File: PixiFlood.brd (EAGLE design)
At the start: 43.2 x 46 mm, 36 parts, among them IC1 WS2811-SOP8, IC2 78L05Z, T1 2N3904, T2 2N3904, T3 2N3904, U1 PT4115B89E, U2 PT4115B89E, U3 PT4115B89E, X2 22-23-2041

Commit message: Initial Commit
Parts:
- removed T$1, T$2, T$3, T$4, T$5, T$6, T$7, T$8, T$9: TEST_PINTP-2, headers:TP-2
- removed T1, T2, T3: 2N3904, transistor:TO92
- removed X2: 22-23-2041, connectors:22-23-2041
- added C3: .1uF, capacitors:EIA3216
- added C4: 10uF, capacitors:VISHAY-CASE-D
- added IC3: TC7W04FP-0.65, logic:SSOP8-0.65P-(TSSOP8)
- added TP1, TP2, TP3, TP4, TP5, TP6, TP7, TP9: TPSQTP15R, testpad:TP15R
- added TP8: TPSQTP20SQ, testpad:TP20SQ
- added X1: 22-23-2041, connectors:22-23-2041
- B1: value LED-BOARDNODIM -> LED-BOARDV4; device myBoards:LED_BOARD_V5_A -> special:LED_BOARD-V4
- C1: value 100uF -> 10uF; device rcl:TT2D6L -> capacitors:VISHAY-CASE-D
- C2: value .1uF -> 10uF; device rcl:C050-024X044 -> capacitors:VISHAY-CASE-D
- D1, D2, D3: value 1N5819 -> B340A; device diode:DO07 -> SparkFun-DiscreteSemi:SMA-DIODE
- IC1: value WS2811-SOP8 -> 78L05SMD; device MyLibrary:SO08-SKINNYPADS -> regulators:SO08
- IC2: value 78L05Z -> WS2811S; device linear:TO92 -> drivers:SO08
- L1, L2, L3: value INDUCTOR82114R -> SLF7045T-101MR60-H; device rcl:82114R-C -> inductors:SLF7045
- R1: value .3R -> .33R; device resistor:0204/7 -> resistor:R1210
- R2, R3: value .3R -> 33R; device resistor:0204/7 -> rcl:R1206
- R4: value 4.7k -> 100; device resistor:0204/7 -> rcl:R1206
- R5, R6: value 4.7k -> .33R; device resistor:0204/7 -> resistor:R1210
- R7, R9: value 33R -> 4.7k; device rcl:0204/7 -> rcl:R1206
- R8: value 100R -> 4.7k; device rcl:0204/7 -> rcl:R1206
- moved R3 31.3 mm to (39.9, 42.2)
- moved C2 22.5 mm to (22.0, 14.0), turned to 0 degrees
- moved R2 21.2 mm to (36.4, 42.0)
- moved R1 16.8 mm to (27.8, 26.2)
- moved R4 13.8 mm to (33.1, 42.0), flipped to the top
- moved R5 13.8 mm to (27.8, 17.7), flipped to the top, turned to 270 degrees
- moved IC1 13.7 mm to (24.4, 36.2), turned to 90 degrees
- moved R6 13.6 mm to (27.9, 9.43), flipped to the top
- moved R7 11.1 mm to (31.0, 34.0)
- moved C1 8.82 mm to (21.8, 22.4), turned to 0 degrees
- moved IC2 8.57 mm to (38.0, 36.3), turned to 0 degrees
- moved U3 8.46 mm to (32.1, 9.52)
- moved U2 8.22 mm to (32.1, 17.9)
- moved U1 7.73 mm to (32.1, 26.3)
- moved L3 7.47 mm to (38.6, 6.22), turned to 0 degrees
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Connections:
- removed net +12V: C1.+, D1.C, D2.C, D3.C, IC2.3, R1.1, R2.1, R3.1, T$9.P$1, U1.5, U2.5, U3.5, X2.1
- removed net DIN-R: IC1.6, R9.2
- removed net DO-R: IC1.5, R7.2
- removed net N$15: IC1.3, R6.2, T$5.P$1, T3.2
- removed net N$18: IC1.2, R5.2, T$4.P$1, T2.2
- removed net N$20: IC1.1, R4.2, T$1.P$1, T1.2
- new net BLU-WS: IC2.3, IC3.1, R7.2, TP2.TP
- new net DIN-E: R2.1, X1.3
- new net DO-E: R3.1, X1.4
- new net GREN-WS: IC2.2, IC3.6, R8.2, TP3.TP
- new net RED-WS: IC2.1, IC3.3, R9.2, TP7.TP
- new net VIN: C1.1, C2.1, C4.1, D1.C, D2.C, D3.C, IC1.8, R1.2, R5.2, R6.2, TP4.TP, U1.5, U2.5, U3.5, X1.1
- net +5V: now also C3.A, IC1.1, IC3.8, R7.1, R9.1, TP5.TP; no longer C2.1, IC2.1, R5.1, R6.1, T$2.P$1
- net BLUE: now also IC3.7, TP9.TP; no longer T$6.P$1, T3.1
- net BOUT: now also R6.1; no longer R3.2
- net DIN: now also IC2.6, R2.2; no longer R9.1, X2.3
- net DO: now also IC2.5, R3.2; no longer R7.1, X2.4
- net GND: now also C1.2, C3.C, C4.2, IC1.2, IC1.3, IC1.6, IC1.7, IC2.4, IC3.4, TP8.TP, X1.2; no longer C1.-, IC1.4, IC2.2, T$3.P$1, T1.3, T2.3, T3.3, X2.2
- net GOUT: now also R5.1; no longer R2.2
- net GREEN: now also IC3.2, TP6.TP; no longer T$7.P$1, T2.1
- net N$1: no longer L1.1@A
- net N$10: no longer L3.2@A
- net N$2: no longer L3.1@A
- net N$3: no longer L1.2@A
- net N$5: no longer L2.1@A
- net N$9: no longer L2.2@A
- net RED: now also IC3.5, TP1.TP; no longer T$8.P$1, T1.1
- net ROUT: now also R1.1; no longer R1.2
- net VDD: now also IC2.8, R4.2; no longer IC1.8, R8.2
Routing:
- net +12V: track 99.4 -> 0.00 mm
- net VIN: track 0.00 -> 78.1 mm, vias 0 -> 5
- net N$15: track 37.8 -> 0.00 mm, vias 1 -> 0
- net +5V: track 51.6 -> 29.6 mm
- net N$20: track 19.3 -> 0.00 mm
- net RED-WS: track 0.00 -> 16.9 mm
- net N$18: track 16.3 -> 0.00 mm
- net GREN-WS: track 0.00 -> 15.8 mm
- net BLU-WS: track 0.00 -> 14.3 mm
- net RED: track 21.0 -> 8.58 mm
- net DIN-E: track 0.00 -> 11.8 mm
- net DO-E: track 0.00 -> 11.6 mm
- net DO-R: track 11.1 -> 0.00 mm
- net ROUT: track 39.7 -> 50.7 mm
- net BLUE: track 17.7 -> 26.8 mm, vias 0 -> 2
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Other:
- board size 43.2 x 46 mm -> 43 x 46 mm
- board text added: "+"
- board text added: "-"
- board text added: "12v"
- board text added: "B"
- board text added: "DI"
- board text added: "G"
- board text added: "PixiFlood 10W"
- board text added: "R"
- board text added: "v2.0"
- board text removed: "12V"
- board text removed: "DIN"
- board text removed: "GND"
- board text removed: "PixiFlood"
- board text removed: "V1.11"

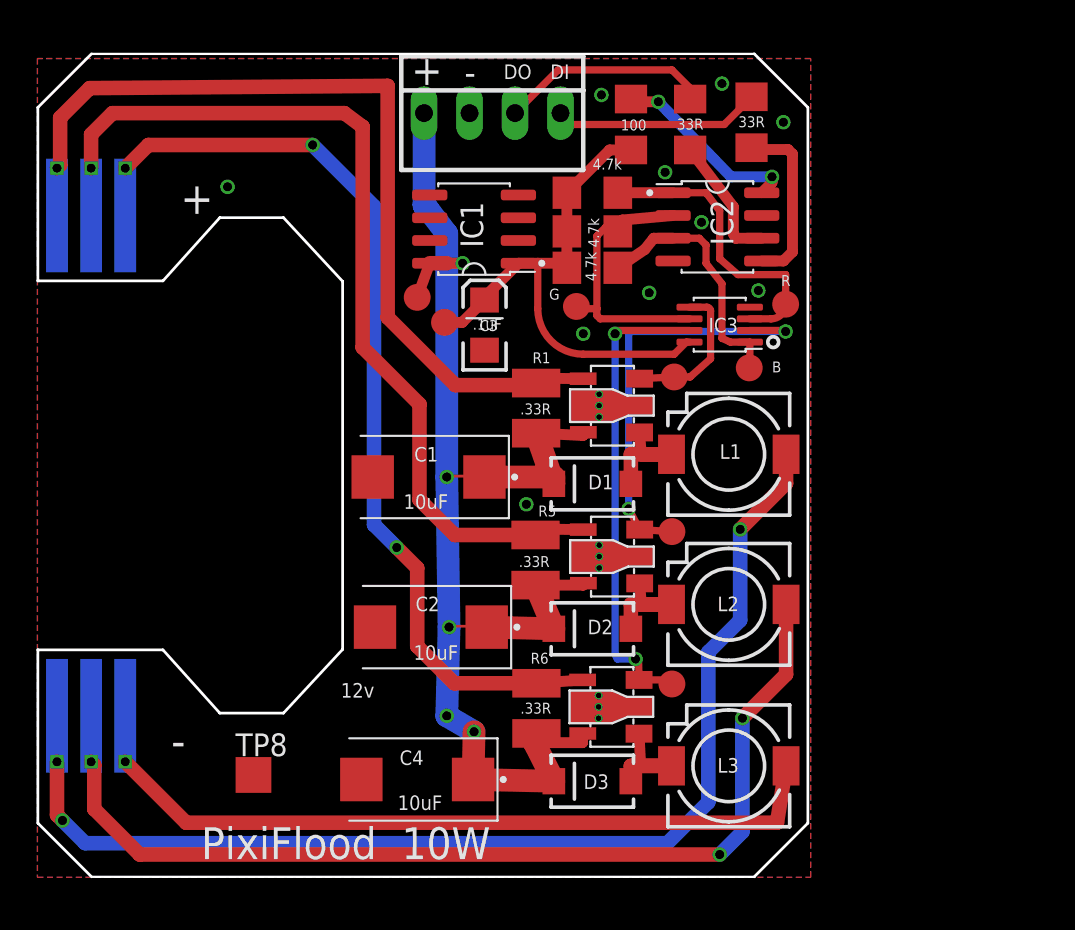
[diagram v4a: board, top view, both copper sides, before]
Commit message: Reworked layout
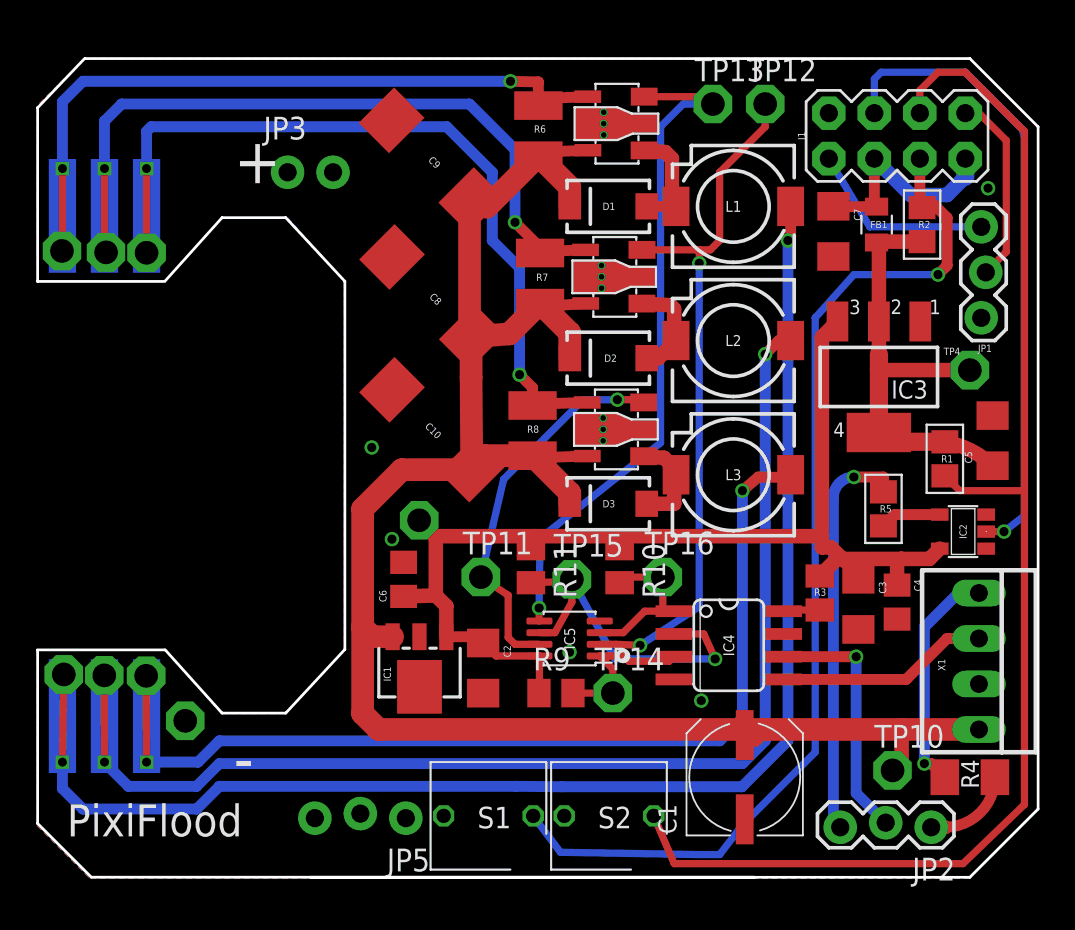
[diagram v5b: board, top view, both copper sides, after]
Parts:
- added C10, C8, C9: 10uF, rcl:SMC_D
- added C5, C7: 10uF, rcl:C1206
- added C6: .1uF, rcl:C0805
- added FB1: BLM21PG221SN1D, ELL-i-Passives:SMD0805-A
- added IC4: WS2811SOP8, drivers:SOP08-P-1.27
- added IC5: TC7W04FP-0.65, logic:SSOP8-0.65P-(TSSOP8)
- added J1: (no value), connectors:2X4
- added JP1, JP2: (no value), connectors:1X03_LOCK
- added JP3: M02NO_SILK, connectors:1X02_NO_SILK
- added JP5: (no value), connectors:1X03_LOCK_NO_SILK
- added R10, R11: 4.7kohm, rcl:M0805
- added S1, S2: SP, switch:TACT_5MM
- added TP10, TP11, TP12, TP13, TP14, TP15, TP16: TPSQPAD1-13, testpad:P1-13
- B1: value LED-BOARDV4 -> LED-BOARDRF; device special:LED_BOARD-V4 -> myBoards:RF_BOARD
- C1: value 10uF -> (none); device capacitors:VISHAY-CASE-D -> rcl:UD-6,3X5,8_NICHICON
- C2: device capacitors:VISHAY-CASE-D -> rcl:C1206
- C3: value .1uF -> 10uF; device capacitors:EIA3216 -> rcl:C1206
- C4: value 10uF -> .1uF; device capacitors:VISHAY-CASE-D -> rcl:C0805
- D1, D2, D3: value B340A -> MBRA140
- IC1: value 78L05SMD -> L78LXXCU/BU; device regulators:SO08 -> regulators:SOT89
- IC2: value WS2811S -> 74LVC1G125DBV; device drivers:SO08 -> logic:SOT23-5
- IC3: value TC7W04FP-0.65 -> LM1117-SOT223; device logic:SSOP8-0.65P-(TSSOP8) -> regulators:SOT223
- R1: value .33R -> 10K; device resistor:R1210 -> resistors:R0805
- R2: value 33R -> 10K; device rcl:R1206 -> resistors:R0805
- R3: value 33R -> 100ohm; device rcl:R1206 -> rcl:M0805
- R4: value 100 -> 33R; device rcl:R1206 -> rcl:M1206
- R5: value .33R -> 100; device resistor:R1210 -> resistors:R0805
- R6: value .33R -> .3ohm .25w; device resistor:R1210 -> rcl:R1210
- R7: value 4.7k -> .3hm .25w; device rcl:R1206 -> rcl:R1210
- R8: value 4.7k -> .3ohm .25w; device rcl:R1206 -> rcl:R1210
- R9: value 4.7k -> 4.7kohm; device rcl:R1206 -> rcl:M0805
- TP1, TP2, TP3, TP4, TP5, TP6, TP7, TP9: value TPSQTP15R -> TPSQPAD1-13; device testpad:TP15R -> testpad:P1-13
- TP8: value TPSQTP20SQ -> TPSQPAD1-13; device testpad:TP20SQ -> testpad:P1-13
- moved R4 41.1 mm to (52.1, 5.59), turned to 0 degrees
- moved X1 40.9 mm to (52.6, 12.1), turned to 270 degrees
- moved TP2 37.2 mm to (8.26, 8.74), turned to 180 degrees
- moved TP7 35.8 mm to (6.10, 34.9)
- moved TP9 34.0 mm to (1.47, 11.3), turned to 180 degrees
- moved R6 32.3 mm to (28.0, 41.7)
- moved TP4 31.1 mm to (52.1, 28.3)
- moved TP6 30.4 mm to (6.07, 11.3)
- moved TP3 28.9 mm to (1.37, 35.0)
- moved C4 28.6 mm to (48.0, 15.4), turned to 270 degrees
- moved R9 28.0 mm to (29.0, 10.3)
- moved R3 26.6 mm to (43.7, 15.9), turned to 90 degrees
- moved C3 26.1 mm to (45.8, 15.2), turned to 270 degrees
- moved IC1 24.7 mm to (21.3, 11.7), turned to 180 degrees
- moved C1 24.3 mm to (39.5, 5.59), turned to 90 degrees
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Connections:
- removed net BLU-WS: IC2.3, IC3.1, R7.2, TP2.TP
- removed net DIN-E: R2.1, X1.3
- removed net DO-E: R3.1, X1.4
- removed net GREN-WS: IC2.2, IC3.6, R8.2, TP3.TP
- removed net N$10: B1.B-, B1.B-@1, L3.2
- removed net N$9: B1.G-, B1.G-@1, L2.2
- removed net RED-WS: IC2.1, IC3.3, R9.2, TP7.TP
- removed net VIN: C1.1, C2.1, C4.1, D1.C, D2.C, D3.C, IC1.8, R1.2, R5.2, R6.2, TP4.TP, U1.5, U2.5, U3.5, X1.1
- new net +12V: C1.+, C10.+, C8.+, C9.+, D1.C, D2.C, D3.C, IC1.3, R6.2, R7.2, R8.2, TP10.TP, U1.5, U2.5, U3.5, X1.4
- new net +3V3: C5.1, FB1.P$1, IC3.2, IC3.4, R1.2, R2.1, TP4.TP
- new net DIN-W: R4.1, X1.1
- new net GPIO0: J1.6, R1.1, S2.1
- new net GPIO2: IC2.2, J1.4
- new net LED-B-NEG: B1.B-2, B1.B-@1, L3.2, TP6.TP
- new net LED-G-NEG: B1.G-2, B1.G-@1, L2.2, TP8.TP
- new net LED-R-NEG: B1.R-2, B1.R-@1, L1.2, TP9.TP
- new net N$16: IC4.3, IC5.1, R9.2, TP14.TP
- new net N$4: IC4.2, IC5.6, R11.2, TP15.TP
- new net N$6: IC2.4, R5.2
- new net RST: J1.5, R2.2, S1.1
- new net RX: J1.8, JP1.2
- new net TX: J1.1, JP1.3
- new net VCC: C7.1, FB1.P$2, J1.3, J1.7
- new net WIFI: JP2.3, R5.1
- new net WIRED: JP2.1, R4.2
- net +5V: now also C2.1, C3.1, C4.1, C6.1, IC2.5, IC3.3, IC5.8, R10.1, R11.1, R3.2, TP1.TP; no longer C3.A, IC3.8, R4.1, R7.1, R8.1, TP5.TP
- net BLUE: now also IC5.7, TP11.TP; no longer IC3.7, TP9.TP
- net BOUT: now also B1.B+2, B1.B+@1, R8.1, TP7.TP; no longer B1.B+, B1.B+@2, R6.1
- net DIN: now also IC4.6, JP2.2; no longer IC2.6, R2.2
- net DO: now also IC4.5, X1.2; no longer IC2.5, R3.2
- net GND: now also C1.-, C10.-, C3.2, C5.2, C6.2, C7.2, C8.-, C9.-, IC1.4, IC2.1, IC2.3, IC3.1, IC4.4, IC5.4, J1.2, JP1.1, JP3.1, JP3.2, JP5.1, JP5.2, JP5.3, S1.2, S2.2, TP2.TP, X1.3; no longer C1.2, C3.C, IC1.3, IC1.6, IC1.7, IC2.4, IC3.4, TP8.TP, X1.2
- net GOUT: now also B1.G+2, R7.1, TP5.TP; no longer B1.G+, R5.1
- net GREEN: now also IC5.2, TP12.TP; no longer IC3.2, TP6.TP
- net N$3: now also IC4.1, IC5.3, R10.2, TP16.TP; no longer B1.R-, B1.R-@1, L1.2
- net RED: now also IC5.5, TP13.TP; no longer IC3.5, TP1.TP
- net ROUT: now also B1.R+2, R6.1, TP3.TP; no longer B1.R+, R1.1
- net VDD: now also IC4.8, R3.1; no longer IC2.8, R4.2
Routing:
- net +12V: track 0.00 -> 109.3 mm
- net LED-R-NEG: track 0.00 -> 81.4 mm, vias 0 -> 1
- net VIN: track 78.1 -> 0.00 mm, vias 5 -> 0
- net GPIO0: track 0.00 -> 75.1 mm
- net LED-G-NEG: track 0.00 -> 69.3 mm, vias 0 -> 1
- net RST: track 0.00 -> 59.4 mm, vias 0 -> 1
- net LED-B-NEG: track 0.00 -> 57.4 mm, vias 0 -> 1
- net N$9: track 56.8 -> 0.00 mm, vias 2 -> 0
- net N$3: track 64.7 -> 9.87 mm, vias 2 -> 0
- net N$10: track 43.6 -> 0.00 mm
- net +5V: track 29.6 -> 66.3 mm
- net GPIO2: track 0.00 -> 35.7 mm, vias 0 -> 1
- net RED: track 8.58 -> 38.3 mm, vias 0 -> 1
- net +3V3: track 0.00 -> 25.1 mm
- net WIFI: track 0.00 -> 22.7 mm, vias 0 -> 1
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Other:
- board size 43 x 46 mm -> 55.9 x 45.7 mm
- board text added: "PixiFlood"
- board text added: "WiFi V1.1"
- board text removed: "+"
- board text removed: "-"
- board text removed: "12v"
- board text removed: "B"
- board text removed: "DI"
- board text removed: "DO"
- board text removed: "G"
- board text removed: "PixiFlood 10W"
- board text removed: "R"
- board text removed: "v2.0"

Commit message: Reworked layout
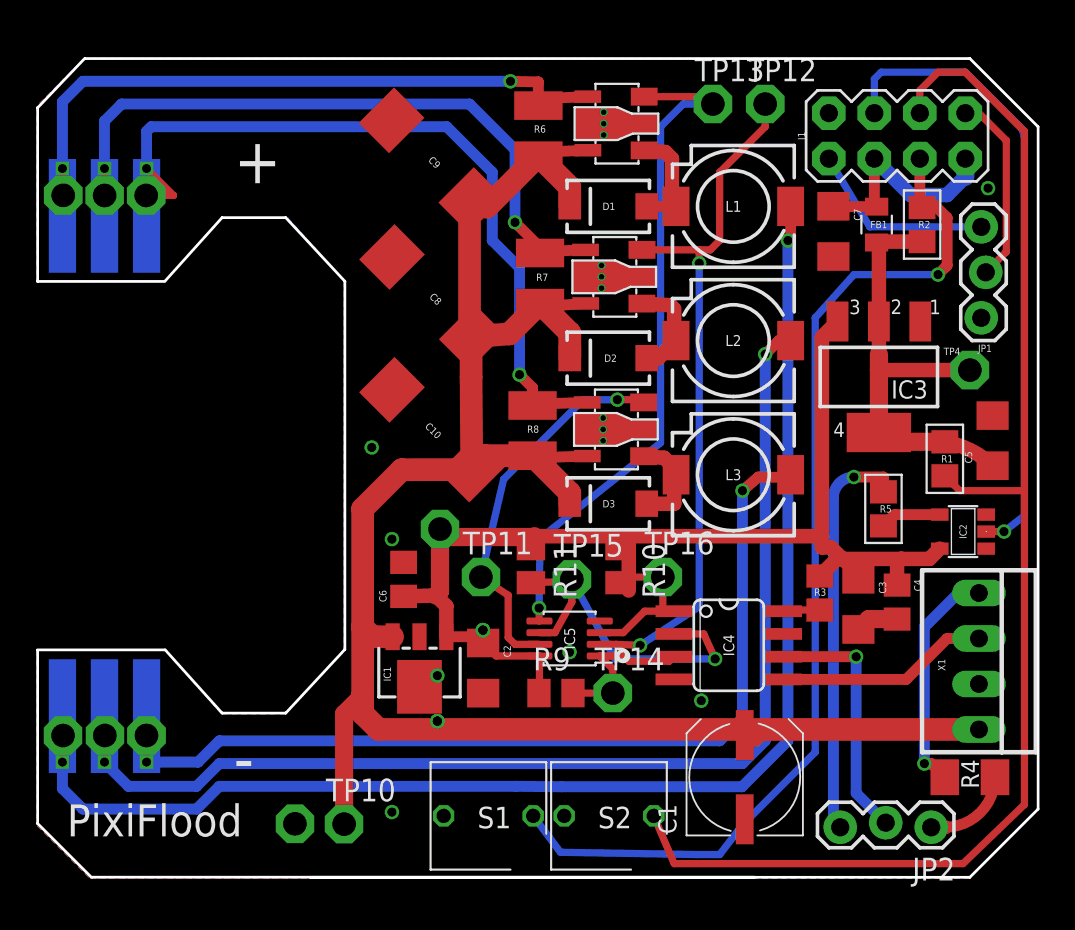
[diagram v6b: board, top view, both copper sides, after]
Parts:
- removed JP3: M02NO_SILK, connectors:1X02_NO_SILK
- removed JP5: (no value), connectors:1X03_LOCK_NO_SILK
- R3: device rcl:M0805 -> rcl:R0805
- moved TP10 30.8 mm to (17.1, 2.97)
- moved TP2 8.40 mm to (14.4, 2.99)
- moved TP9 3.41 mm to (1.43, 7.92)
- moved TP8 3.36 mm to (3.77, 7.92)
- moved TP6 3.33 mm to (6.09, 7.92)
- moved TP7 3.20 mm to (6.07, 38.1)
- moved TP5 3.17 mm to (3.75, 38.1)
- moved TP3 3.11 mm to (1.44, 38.1)
- moved TP1 1.26 mm to (22.5, 19.4)
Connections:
- net GND: no longer JP3.1, JP3.2, JP5.1, JP5.2, JP5.3
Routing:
- net +12V: track 109.3 -> 114.4 mm
- net LED-R-NEG: track 81.4 -> 78.0 mm
- net LED-G-NEG: track 69.3 -> 65.9 mm
- net LED-B-NEG: track 57.4 -> 54.1 mm
- net GOUT: track 43.3 -> 40.1 mm
- net ROUT: track 42.3 -> 39.2 mm
- net GND: track 0.00 -> 2.40 mm, vias 5 -> 11
- net BOUT: track 46.9 -> 45.9 mm
- net +5V: track 66.3 -> 67.2 mm
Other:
- board text added: "V1.2w"
- board text removed: "WiFi V1.1"

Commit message: Reworked layout
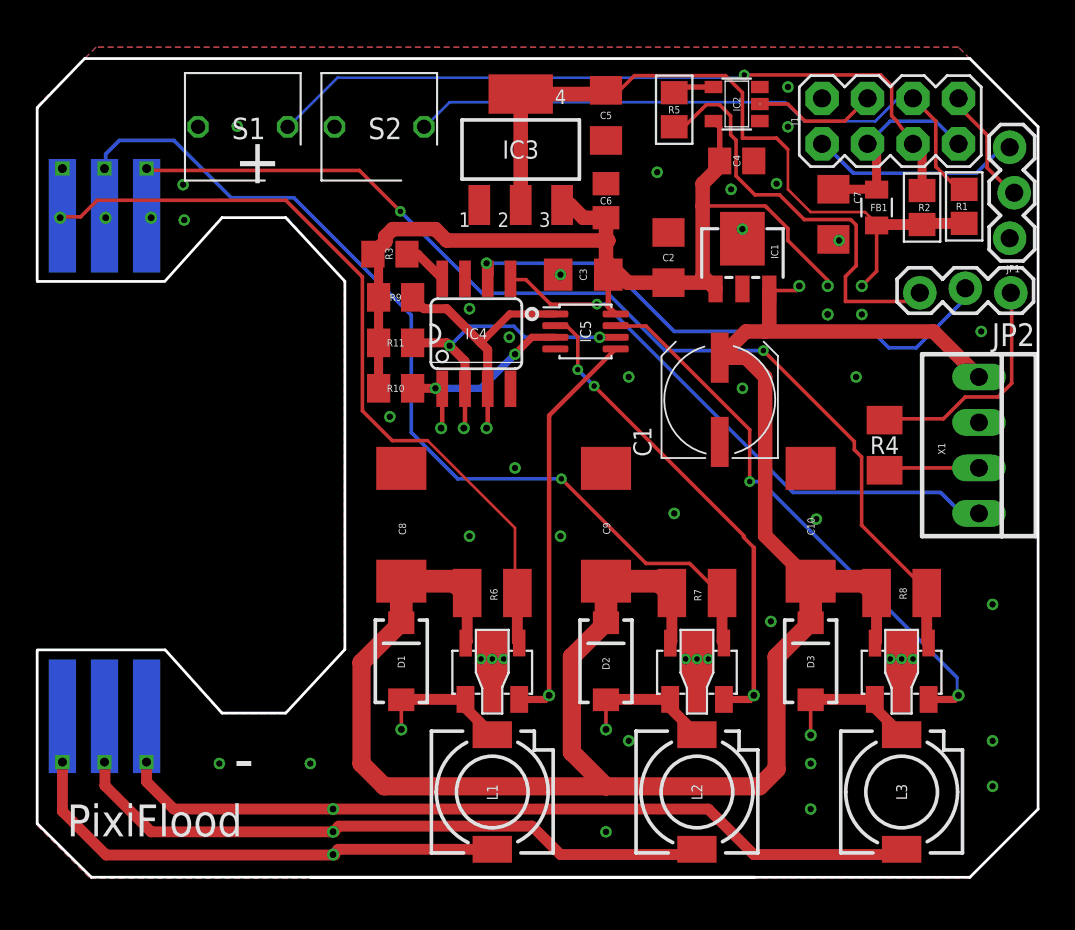
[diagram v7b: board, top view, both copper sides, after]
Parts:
- removed TP11, TP12, TP13, TP14, TP15, TP16, TP4, TP5, TP6, TP7, TP8, TP9: TPSQPAD1-13, testpad:P1-13
- added TP17, TP18, TP19, TP20, TP21, TP22, TP23, TP24, TP25, TP26, TP27, TP28, TP29, TP30, TP31: TEST-POINTTP_15TH_THRU, SparkFun-Connectors:TP_15TH
- TP1, TP10, TP2, TP3: value TPSQPAD1-13 -> TEST-POINTTP_15TH_THRU; device testpad:P1-13 -> SparkFun-Connectors:TP_15TH
- moved S1 40.9 mm to (14.0, 41.9)
- moved S2 40.6 mm to (21.6, 41.9)
- moved TP10 40.4 mm to (44.1, 33.0)
- moved L1 35.4 mm to (25.4, 4.76), turned to 270 degrees
- moved TP3 35.3 mm to (20.3, 8.26)
- moved U1 31.4 mm to (25.4, 11.4), turned to 0 degrees
- moved R3 30.6 mm to (19.7, 34.8), turned to 180 degrees
- moved JP2 30.2 mm to (54.4, 32.8)
- moved IC1 29.2 mm to (39.4, 34.6), turned to 0 degrees
- moved C5 28.2 mm to (31.8, 42.5), turned to 270 degrees
- moved D1 27.9 mm to (20.3, 12.1), turned to 90 degrees
- moved IC2 27.0 mm to (39.1, 43.2)
- moved C4 26.2 mm to (39.1, 40.0), turned to 0 degrees
- moved R6 25.9 mm to (25.4, 15.9), turned to 180 degrees
- moved L2 25.3 mm to (36.8, 4.76), turned to 270 degrees
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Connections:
- net +12V: now also TP17.P$1, X1.1; no longer TP10.TP, X1.4
- net +3V3: now also TP19.P$1; no longer TP4.TP
- net +5V: now also TP10.P$1; no longer TP1.TP
- net BLUE: now also TP20.P$1; no longer TP11.TP
- net BOUT: now also TP30.P$1; no longer TP7.TP
- net DIN-W: now also X1.3; no longer X1.1
- net DO: now also X1.4; no longer X1.2
- net GND: now also TP18.P$1, X1.2; no longer TP2.TP, X1.3
- net GOUT: now also TP29.P$1; no longer TP5.TP
- net GREEN: now also TP23.P$1; no longer TP12.TP
- net LED-B-NEG: now also TP31.P$1; no longer TP6.TP
- net LED-G-NEG: now also TP28.P$1; no longer TP8.TP
- net LED-R-NEG: now also TP27.P$1; no longer TP9.TP
- net N$1: now also TP3.P$1
- net N$16: now also TP21.P$1; no longer TP14.TP
- net N$2: now also TP1.P$1
- net N$3: now also TP24.P$1; no longer TP16.TP
- net N$4: now also TP22.P$1; no longer TP15.TP
- net N$5: now also TP2.P$1
- net RED: now also TP25.P$1; no longer TP13.TP
- net ROUT: now also TP26.P$1; no longer TP3.TP
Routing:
- net LED-R-NEG: track 78.0 -> 30.8 mm, vias 1 -> 0
- net GPIO0: track 75.1 -> 35.5 mm
- net GPIO2: track 35.7 -> 6.93 mm, vias 1 -> 0
- net LED-G-NEG: track 65.9 -> 39.3 mm, vias 1 -> 0
- net DO: track 11.8 -> 31.6 mm, vias 0 -> 1
- net RST: track 59.4 -> 41.6 mm
- net DIN: track 14.0 -> 31.7 mm
- net +3V3: track 25.1 -> 41.4 mm
- net BOUT: track 45.9 -> 61.8 mm, vias 1 -> 2
- net RED: track 38.3 -> 22.6 mm, vias 1 -> 0
- net GOUT: track 40.1 -> 55.4 mm
- net GREEN: track 39.4 -> 27.4 mm
- net BLUE: track 21.4 -> 31.7 mm
- net +5V: track 67.2 -> 57.2 mm
- net WIRED: track 4.72 -> 13.0 mm
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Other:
- outline, holes or cut-outs redrawn
